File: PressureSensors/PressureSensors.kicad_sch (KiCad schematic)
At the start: 28 parts, among them J1 Conn_02x03_Odd_Even, U1 LPS22HB, U2 LPS22HB, U3 LPS22HB, U4 LPS22HB, U5 PCA9548ADB, U6 K78xxJT-500R3

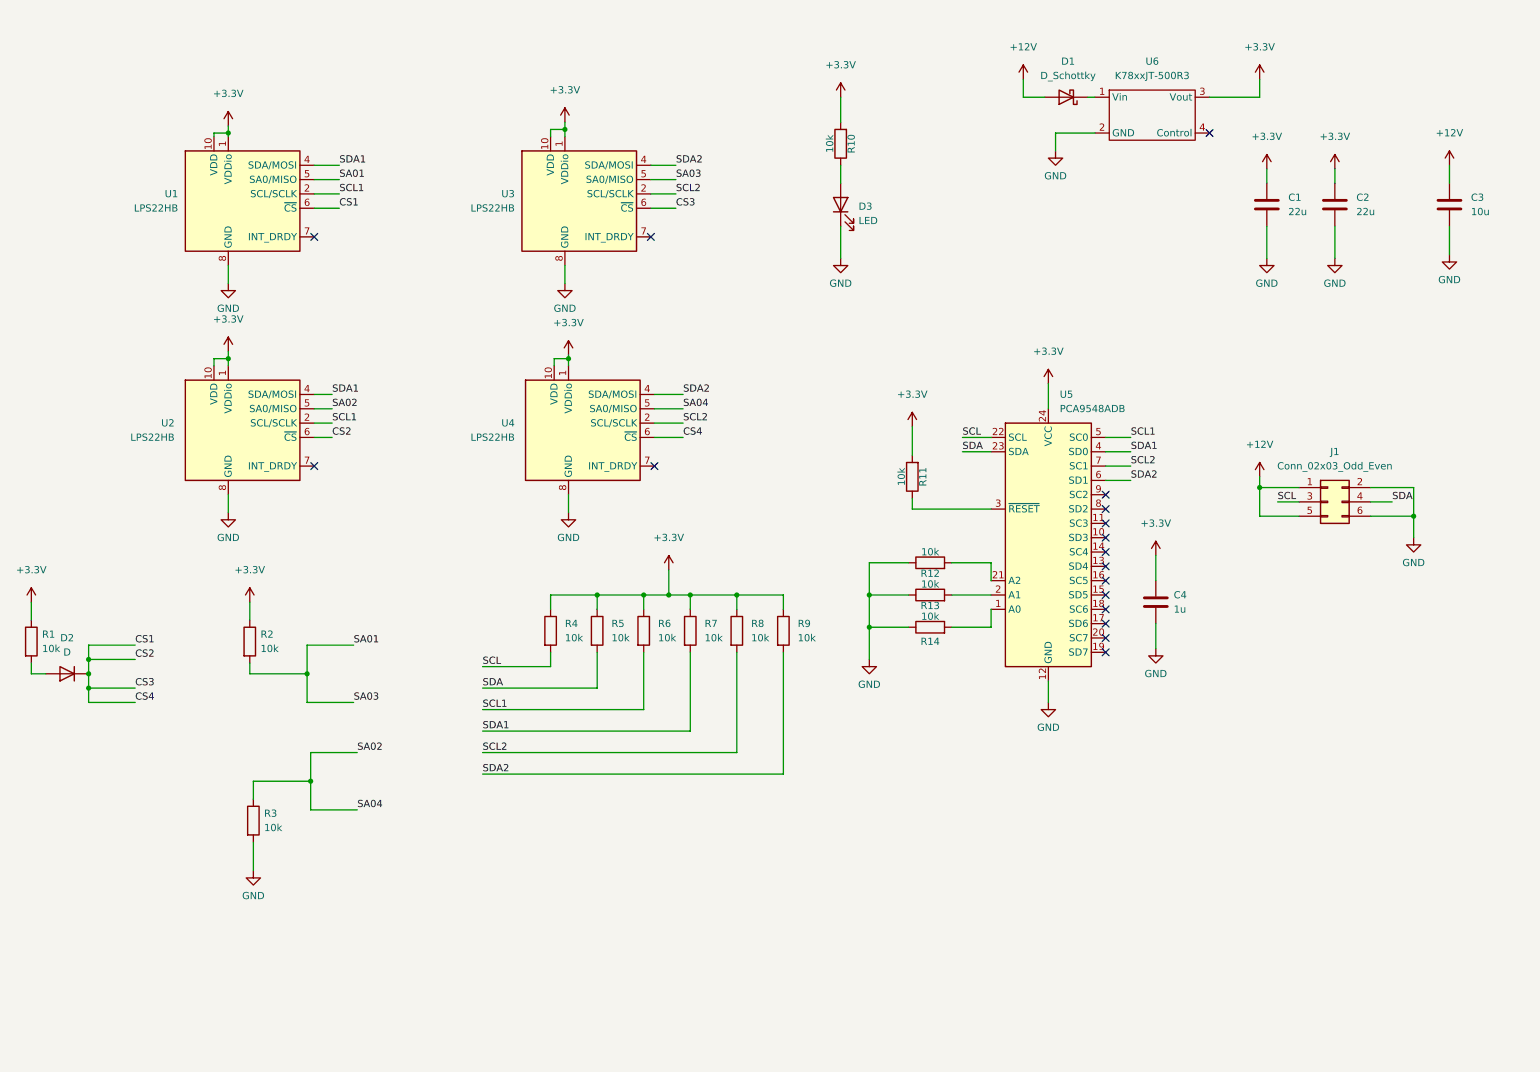
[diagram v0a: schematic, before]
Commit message: Designed Pressure sensors PCB
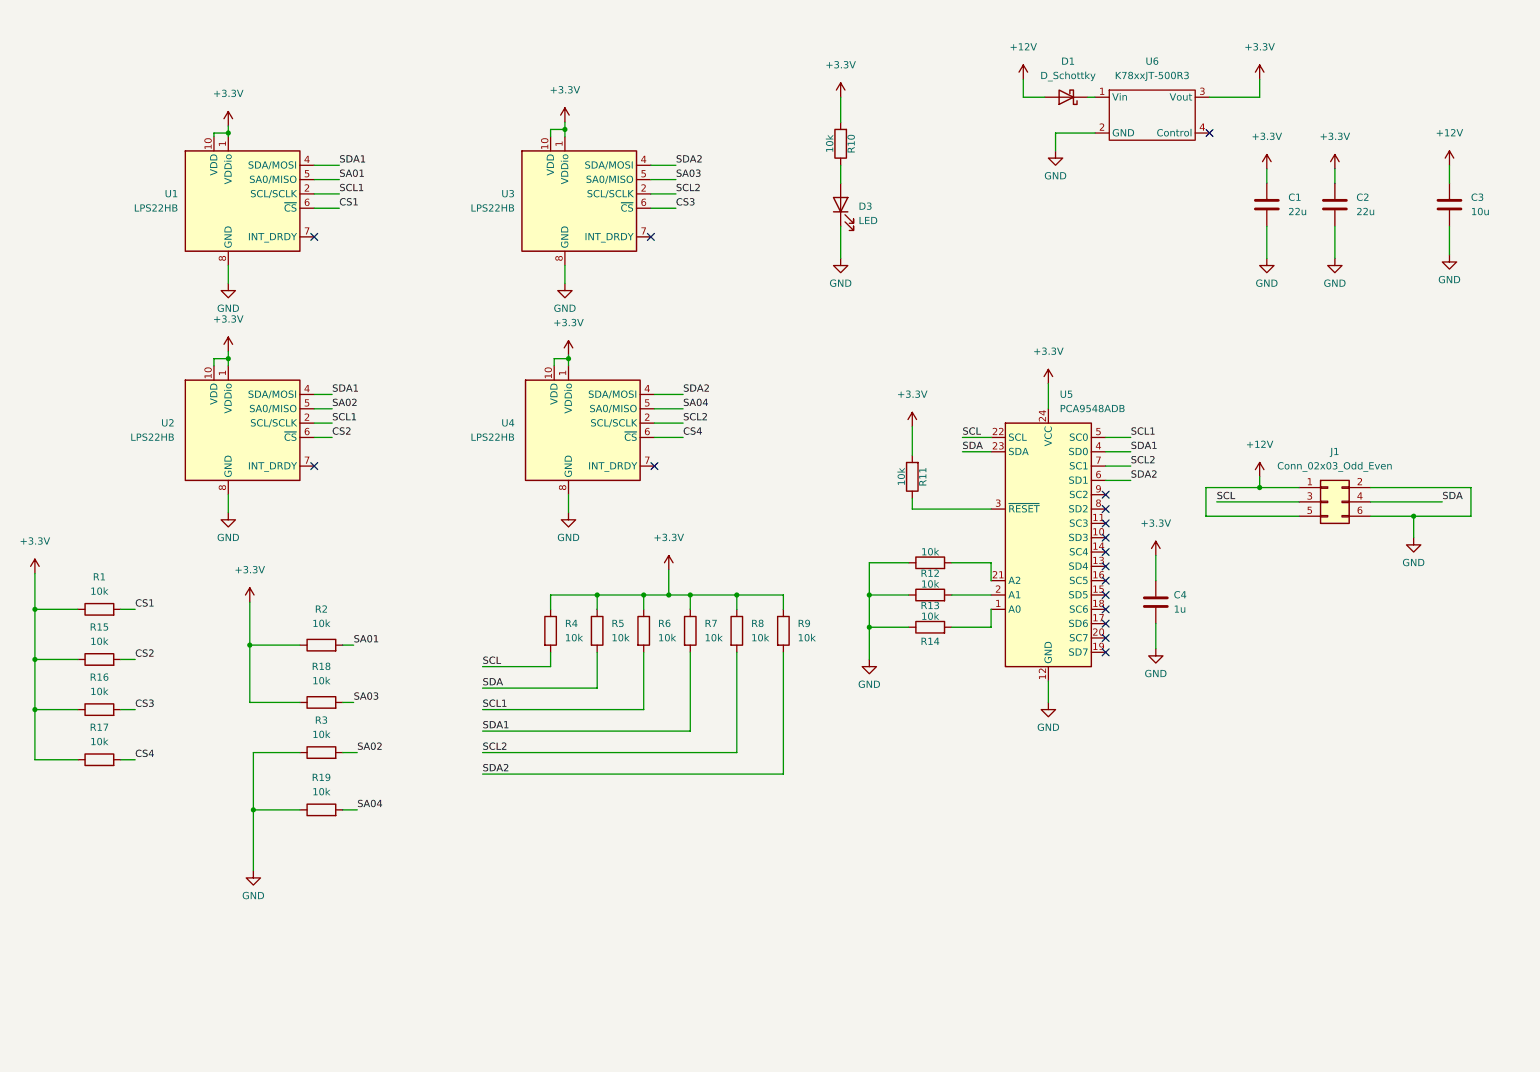
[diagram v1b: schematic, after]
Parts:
- removed D2: D, symbol Device:D
- added R15, R16, R17, R18, R19: 10k, Resistor_SMD:R_0805_2012Metric_Pad1.20x1.40mm_HandSolder, symbol Device:R
- C1, C2, C3, C4: footprint (none) -> Capacitor_SMD:C_0805_2012Metric_Pad1.18x1.45mm_HandSolder
- D1: footprint (none) -> Diode_SMD:D_SMA
- D3: footprint (none) -> LED_SMD:LED_0805_2012Metric_Pad1.15x1.40mm_HandSolder
- J1: footprint (none) -> Connector_PinHeader_2.54mm:PinHeader_2x03_P2.54mm_Vertical
- R1, R10, R11, R12, R13, R14, R2, R3, R4, R5, R6, R7, R8, R9: footprint (none) -> Resistor_SMD:R_0805_2012Metric_Pad1.20x1.40mm_HandSolder
- U6: footprint (none) -> Custom:K7803JT-500R3-SMD
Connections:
- net +3V3: now also R15.1, R16.1, R17.1, R18.1
- net CS1: now also R1.2; no longer U2.6 (~{CS}), U3.6 (~{CS}), U4.6 (~{CS})
- net GND: now also R3.1, R19.1; no longer R3.2
- net SA01: no longer U3.5 (SA0/MISO)
- net SA02: now also R3.2; no longer R3.1, U4.5 (SA0/MISO)
- new net CS2: R15.2, U2.6 (~{CS})
- new net CS3: R16.2, U3.6 (~{CS})
- new net CS4: R17.2, U4.6 (~{CS})
- new net SA03: R18.2, U3.5 (SA0/MISO)
- new net SA04: R19.2, U4.5 (SA0/MISO)
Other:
- moved on the sheet: R1, R2, R3

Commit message: Tidying up design sheets
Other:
- note added: "ADDRESS CONF"
- note added: "CONNECTOR"
- note added: "I2C MODE CONF"
- note added: "I2C MULTIPLEXER"
- note added: "INDICATOR LED"
- note added: "POWER"
- note added: "SENSORS"
- title: (none) -> Mozart Pressure Sensors
- moved on the sheet: C4, J1, R1, R11, R12, R13, R14, R15, R16, R17, R18, R19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

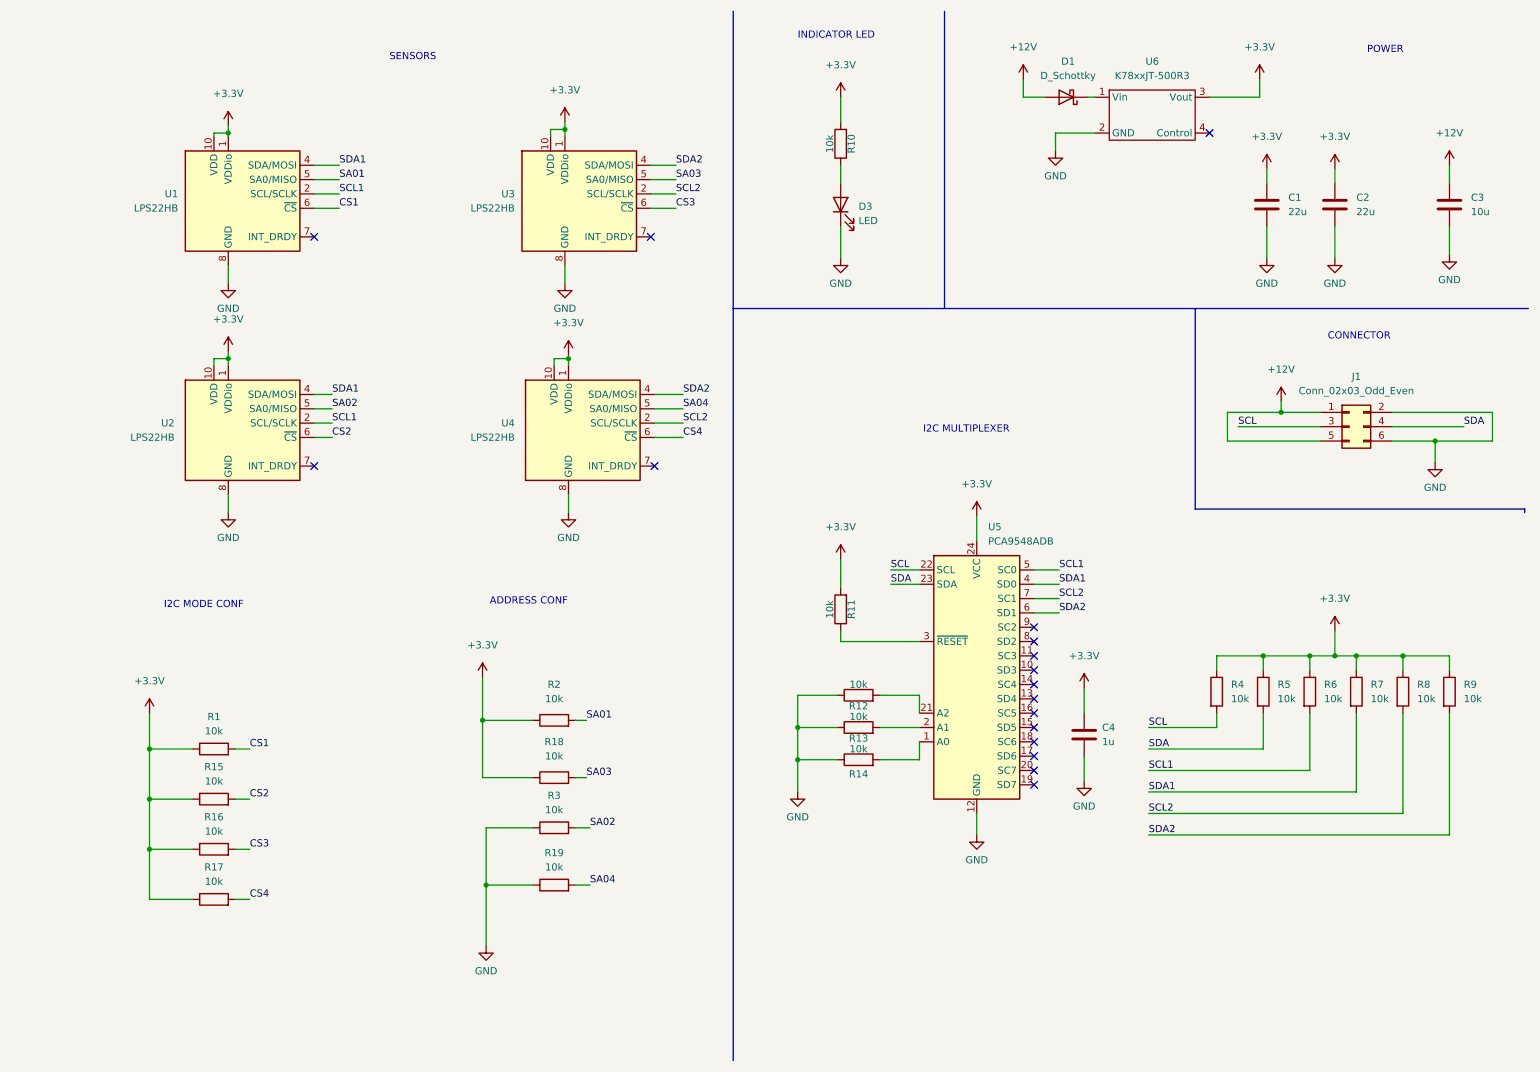
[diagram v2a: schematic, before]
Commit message: Changed I2C multiplexer to 2 channel
Changed power source to LDO

Corrected spacing between sensors

Added missing capacitor for sensors

Eliminated unnecesary resistors for sensors
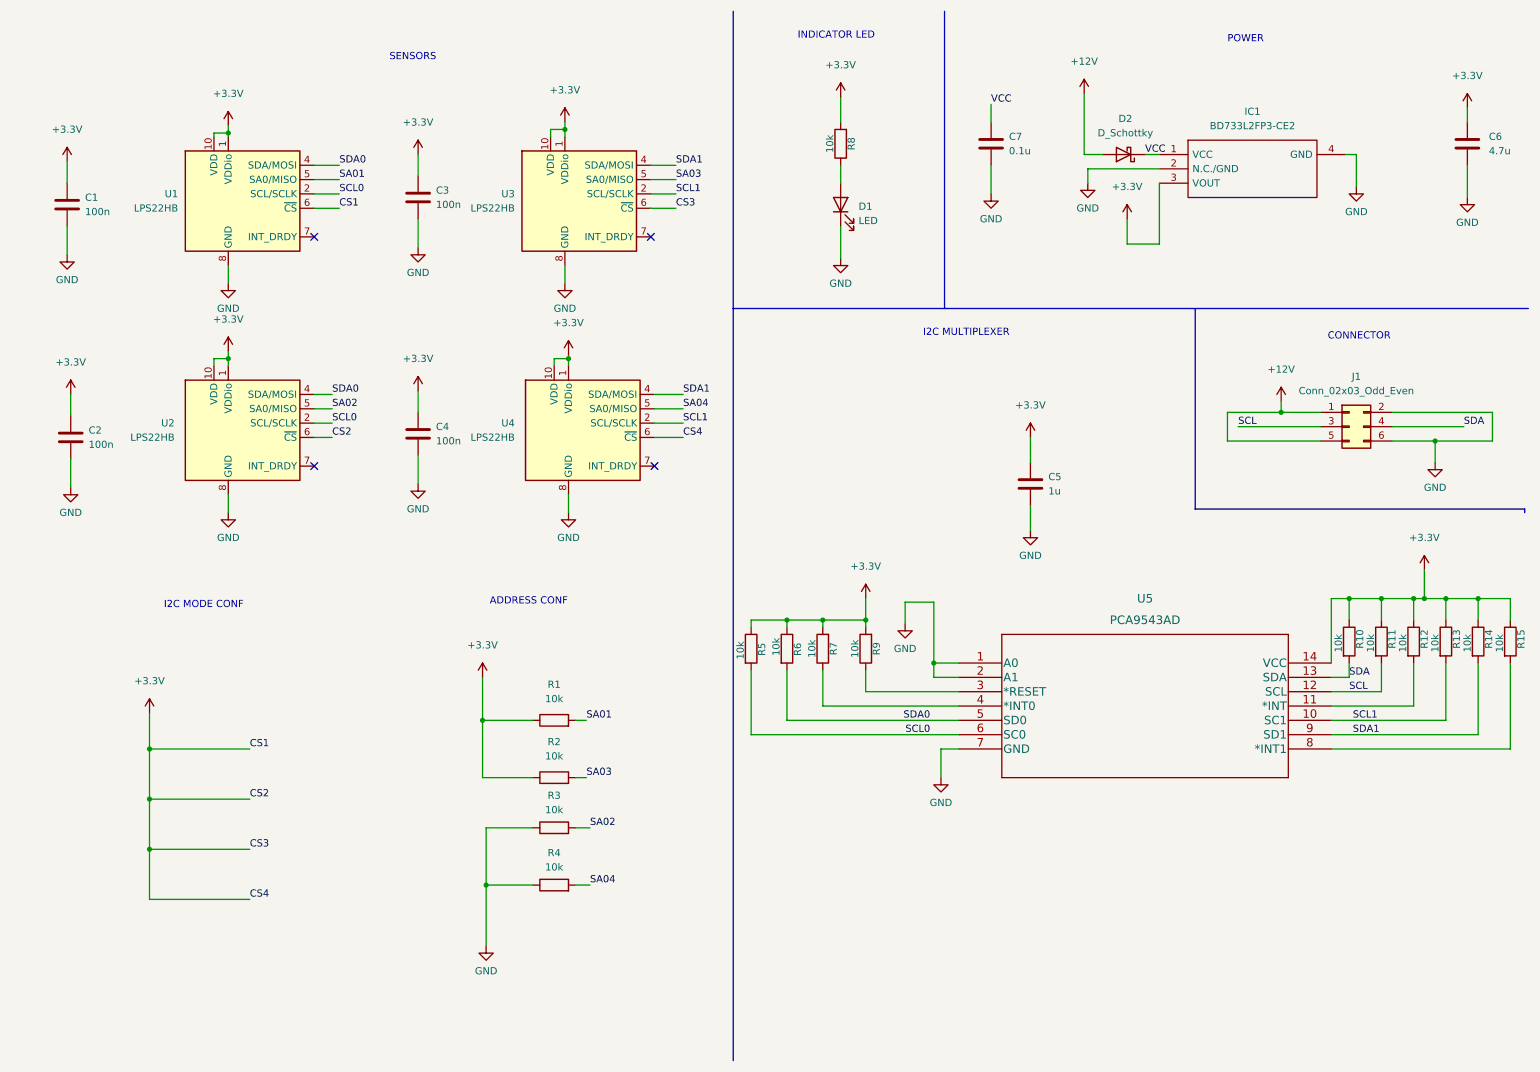
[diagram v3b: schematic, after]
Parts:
- removed R1, R13, R14, R16, R17: 10k, Resistor_SMD:R_0805_2012Metric_Pad1.20x1.40mm_HandSolder, symbol Device:R
- removed U5: PCA9548ADB, Package_SO:SSOP-24_5.3x8.2mm_P0.65mm, symbol Interface_Expansion:PCA9548ADB
- removed U6: K78xxJT-500R3, Custom:K7803JT-500R3-SMD, symbol Custom:K78xxJT-500R3
- added C1, C3, C4: 100n, Capacitor_SMD:C_0805_2012Metric_Pad1.18x1.45mm_HandSolder, symbol Device:C
- added IC1: BD733L2FP3-CE2, Custom:SOT230P700X180-4N, symbol Custom:BD733L2FP3-CE2
- added R7: 10k, Resistor_SMD:R_0805_2012Metric_Pad1.20x1.40mm_HandSolder, symbol Device:R
- added U5: PCA9543AD, Custom:PCA9543AD, symbol Custom:PCA9543AD
- C2: value 22u -> 100n
- C6: renamed from C1; value 22u -> 4.7u
- C7: renamed from C3; value 10u -> 0.1u
- renumbered C4 to C5, D3 to D1, D1 to D2, R2 to R1, R4 to R10, R5 to R11, R8 to R13, R9 to R14, R18 to R2, R19 to R4, R6 to R5, R7 to R6, R10 to R8, R11 to R9
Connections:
- net CS1 is gone; now on net +3V3: U1.6 (~{CS})
- net CS3 is gone; now on net +3V3: U3.6 (~{CS})
- net CS4 is gone; now on net +3V3: U4.6 (~{CS})
- net SCL2 is gone; now on net SCL1: R13.2, U3.2 (SCL/SCLK), U4.2 (SCL/SCLK)
- net SDA2 is gone; now on net SDA1: R14.2, U3.4 (SDA/MOSI), U4.4 (SDA/MOSI)
- net +12V: no longer C7.1
- net +3V3: now also R12.1, U2.6 (~{CS}), C1.1, C3.1, C4.1, IC1.3 (VOUT), R7.2, U5.14 (VCC)
- net GND: now also C1.2, C3.2, C4.2, IC1.2 (N.C./GND), IC1.4 (GND), U5.1 (A0), U5.2 (A1), U5.7 (GND); no longer R12.1
- net SCL: now also R11.2, U5.12 (SCL); no longer R10.2
- net SCL1: now also U5.10 (SC1); no longer R5.2, U1.2 (SCL/SCLK), U2.2 (SCL/SCLK)
- net SDA: now also R10.2, U5.13 (SDA); no longer R11.2
- net SDA1: now also U5.9 (SD1); no longer R6.2, U1.4 (SDA/MOSI), U2.4 (SDA/MOSI)
- net VCC: now reaches D2.1 (K)
- net VCC: now also C7.1, IC1.1 (VCC)
- net at R9.1: now also U5.3 (*RESET)
- net at R12.2: now also U5.11 (*INT)
- net CS2: no longer names the net of R15.2
- net CS2: now also U5.8 (*INT1); no longer U2.6 (~{CS})
- new net: R7.1, U5.4 (*INT0)
- new net SCL0: R5.2, U1.2 (SCL/SCLK), U2.2 (SCL/SCLK), U5.6 (SC0)
- new net SDA0: R6.2, U1.4 (SDA/MOSI), U2.4 (SDA/MOSI), U5.5 (SD0)
- no-connect marks 17 -> 4
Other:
- moved on the sheet: C5, C6, C7, D2, R10, R11, R13, R14, R5, R6, R9

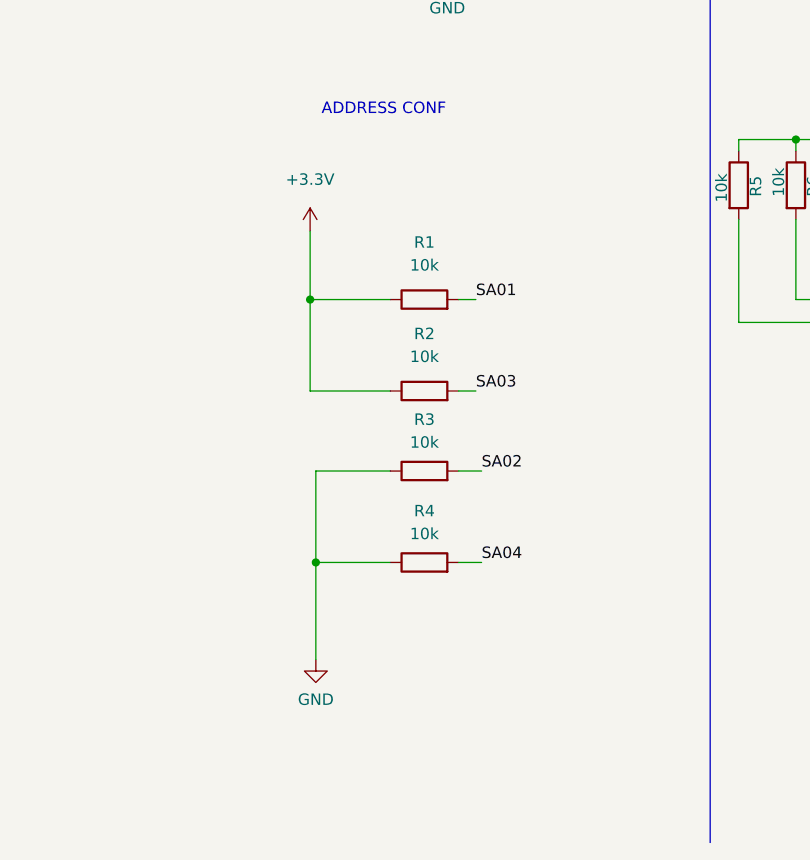
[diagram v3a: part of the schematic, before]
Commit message: Routed with new components
Deleted address selection resistors
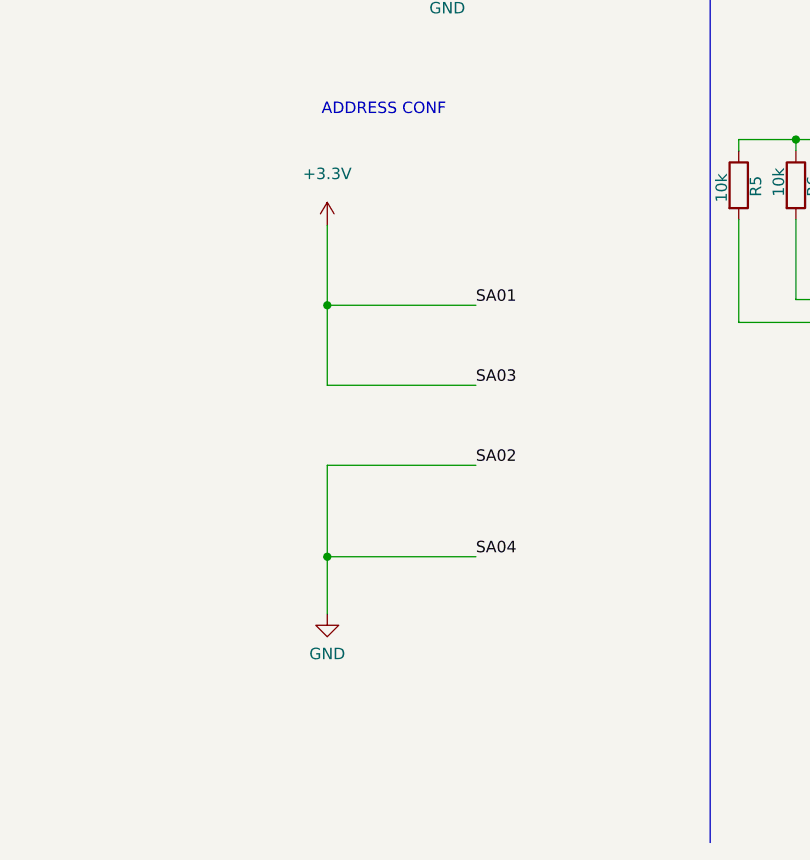
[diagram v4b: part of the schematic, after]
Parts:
- removed R1, R2, R3, R4: 10k, Resistor_SMD:R_0805_2012Metric_Pad1.20x1.40mm_HandSolder, symbol Device:R
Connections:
- net SA01 is gone; now on net +3V3: U1.5 (SA0/MISO)
- net SA02 is gone; now on net GND: U2.5 (SA0/MISO)
- net SA03 is gone; now on net +3V3: U3.5 (SA0/MISO)
- net SA04 is gone; now on net GND: U4.5 (SA0/MISO)
